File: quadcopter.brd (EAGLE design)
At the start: 247.1 x 246.9 mm, 79 parts, among them J1 ISP, U1 ATMEGA128RFA1, Y1 16MHz, Y2 32.768kHz

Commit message: Fixed Schematic but still not able to root 90%
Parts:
- removed A1: ANTENNA2SMD5, SparkFun-RF:ANTENNA-CHIP5
- removed B1: 748421245, SparkFun-RF:BALUN
- removed C24, C25: 10nF, quadparts_prebuilt:CAPC2012X140_HS
- removed C26, C28: 100nF, quadparts_prebuilt:CAPC2012X140_HS
- removed C27: 10uF, quadparts_prebuilt:CAPC2012X140_HS
- removed C6: 12pF, SparkFun-Passives:0402-CAP
- removed CG, CG1, CG2, CG3: 1uF, quadparts_prebuilt:CAPC2012X140_HS
- removed D10: Orange, quadparts_prebuilt:LEDSC125X200X120-2_HS
- removed D6: Green, quadparts_prebuilt:LEDSC125X200X120-2_HS
- removed R10, R2: 330, quadparts_prebuilt:RESC2012X60_HS
- removed R8, RG2, RG4, RG6, RG8: 10K, quadparts_prebuilt:RESC2012X60_HS
- removed RG1, RG3, RG5, RG7: 100, quadparts_prebuilt:RESC2012X60_HS
- removed U1: ATMEGA128RFA1, SparkFun-DigitalIC:QFN-64
- removed Y1: 16MHz, SparkFun-FreqCtrl:CRYSTAL-SMD-5X3
- added ANDREW1: LSM9DS1, QuadpartsUpdated:LSM9DS1
- added B2: BALUN0805, quadparts_prebuilt:BALUN
- added C13, C14, C18: 1uF, quadparts_prebuilt:CAPC2012X140_HS
- added C19, C20: 0.1uF, quadparts_prebuilt:CAPC2012X140_HS
- added C21: 0.01uF, quadparts_prebuilt:CAPC2012X140_HS
- added J7, M1, M2, M3, M4: (no value), quadparts_prebuilt:MALE_HEADER_2X1_0.1IN
- added R12, R14, R16, R18: 100, quadparts_prebuilt:RESC2012X60_HS
- added R13, R15, R17, R5, R6: 10K, quadparts_prebuilt:RESC2012X60_HS
- added U2: ATMEGA128RFA1, quadparts_prebuilt:QFN-64
- C1, C2: value 1uF -> 12pF; device SparkFun-Passives:0402-CAP -> quadparts_prebuilt:CAPC2012X140_HS
- C10: value 100nF -> 1uF
- C11: value 22pF -> 1uF; device SparkFun-Passives:0402-CAP -> quadparts_prebuilt:CAPC2012X140_HS
- C12: value 10uF -> 1uF
- C15, C4, C9: device SparkFun-Passives:0402-CAP -> quadparts_prebuilt:CAPC2012X140_HS
- C16: value JUMP -> 1uF; device SparkFun:0402-CAP -> quadparts_prebuilt:CAPC2012X140_HS
- C17: value JUMP -> 10uF; device SparkFun:0402-CAP -> quadparts_prebuilt:CAPC2012X140_HS
- C22: value 1uF -> 22pF
- C3: value 1000uF -> 1uF; device SparkFun-Passives:0402-CAP -> quadparts_prebuilt:CAPC2012X140_HS
- C5: value 12pF -> 220uF; device SparkFun-Passives:0402-CAP -> quadparts_prebuilt:CAPMP7343X310_HS
- C7: value 12pF -> 10uF; device SparkFun-Passives:0402-CAP -> quadparts_prebuilt:CAPC2012X140_HS
- C8: value 12pF -> 0.01uF; device SparkFun-Passives:0402-CAP -> quadparts_prebuilt:CAPC2012X140_HS
- R1: value 10k -> 10K; device SparkFun-Passives:0402-RES -> quadparts_prebuilt:RESC2012X60_HS
- R11: value 100 -> 10K
- U$5: value IMULAST -> ANTENNA2SMD5; device QuadpartsUpdated:LGA-24/4MM -> quadparts_prebuilt:ANTENNA-CHIP5
- Y2: value 32.768kHz -> (none); device SparkFun-FreqCtrl:CRYSTAL-32KHZ-SMD -> quadparts_prebuilt:CRYSTAL-SMD-5X3
- moved C11 288.3 mm to (-191.8, 158.8)
- moved C8 280.3 mm to (-204.5, 149.9), turned to 0 degrees
- moved C16 254.3 mm to (-139.7, 162.6)
- moved C17 251.5 mm to (-149.9, 158.8), turned to 0 degrees
- moved C15 246.9 mm to (-170.2, 154.9), flipped to the top
- moved R1 242.4 mm to (-158.8, 162.6), turned to 0 degrees
- moved C7 233.5 mm to (-142.2, 158.8), turned to 0 degrees
- moved C12 232.1 mm to (-198.1, 158.8), turned to 0 degrees
- moved C23 199.5 mm to (-152.4, 162.6), turned to 0 degrees
- moved RX_R 86.8 mm to (14.7, 28.9), flipped to the bottom, turned to 0 degrees
- moved C3 86.0 mm to (6.70, 35.0), turned to 0 degrees
- moved C4 83.6 mm to (13.4, 31.7), turned to 0 degrees
- moved RX_LED 80.7 mm to (19.1, 30.0), flipped to the bottom, turned to 270 degrees
- moved TX_LED 78.2 mm to (9.93, 30.0), flipped to the bottom, turned to 270 degrees
- moved TX_R 77.2 mm to (10.0, 24.7), flipped to the bottom
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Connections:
- removed net A0: U1.63
- removed net N$10: B1.4, C16.2
- removed net N$11: B1.3, C17.1
- removed net N$25: MOSFET3.1, RG5.1, RG6.1
- removed net N$30: MOSFET4.1, RG7.1, RG8.1
- removed net N$31: D6.A, R2.1
- removed net N$34: R8.2, U$5.5
- removed net N$35: D10.A, R10.1
- removed net N$5: C7.1, U1.18, Y2.X1
- removed net N$6: C8.1, U1.17, Y2.X2
- removed net PG5: U1.19
- removed net TST: U1.11
- new net N$48: MOSFET2.1
- new net N$50: MOSFET3.1
- new net N$52: C18.1, MOSFET4.1, R17.2, R18.2
- new net VBAT_SENSE: R5.1, R6.2, U2.63
- net 3V: now also ANDREW1.P$1, ANDREW1.P$13, ANDREW1.P$22, ANDREW1.P$23, ANDREW1.P$3, ANDREW1.P$5, ANDREW1.P$6, ANDREW1.P$7, ANDREW1.P$8, C16.1, C17.2, C19.2, J7.1, U2.23, U2.34, U2.44, U2.54, U2.59; no longer C23.1, C26.2, C27.2, R8.1, U$5.22, U$5.23, U$5.6, U$5.7, U$5.8, U1.23, U1.34, U1.44, U1.54, U1.59
- net A1: now also U2.64; no longer U1.64
- net A2: now also U2.1; no longer U1.1
- net A3: now also U2.2; no longer U1.2
- net A4: now also U2.3; no longer U1.3
- net A5: now also U2.4; no longer U1.4
- net A6: now also U2.5; no longer U1.5
- net A7: now also U2.6; no longer U1.6
- net AREF: now also U2.62; no longer U1.62
- net AVDD: now also C11.1, U2.60; no longer C1.1, U1.60
- net BAT_GND: now also C5.2, C7.2, C8.2; no longer C12.2, C24.2, D10.C, D6.C, R11.1
- net DVDD: now also C23.1, U2.21, U2.22; no longer C2.1, U1.21, U1.22
- net GND: now also ANDREW1.P$14, ANDREW1.P$15, ANDREW1.P$16, ANDREW1.P$17, ANDREW1.P$18, ANDREW1.P$19, ANDREW1.P$20, B2.5, C12.2, C13.2, C14.2, C16.2, C17.1, C18.2, C19.1, C20.1, C21.2, C22.1, C9.2, J7.2, M1.1, M2.1, M3.1, M4.1, R11.1, R13.1, R15.1, R17.1, R6.1, U2.10, U2.11, U2.20, U2.24, U2.33, U2.35, U2.45, U2.55, U2.58, U2.61, U2.7; no longer B1.5, C22.2, C25.2, C26.1, C27.1, C28.1, C5.2, C6.2, C7.2, C8.2, C9.1, CG.2, CG1.2, CG2.2, CG3.2, R11.2, RG2.2, RG4.2, RG6.2, RG8.2, U$5.14, U$5.15, U$5.16, U$5.17, U$5.18\, U$5.19, U$5.20, U1.10, U1.20, U1.24, U1.33, U1.35, U1.45, U1.55, U1.58, U1.61, U1.65, U1.7
- net MISO: now also U2.39; no longer U1.39
- net MOSI: now also U2.38; no longer U1.38
- net N$15: now also C13.1, R13.2, R14.2; no longer MOSFET1.1, RG1.1, RG2.1
- net N$2: now also MOSFET1.1, R11.2, R12.2; no longer U$5.1, U$5.3
- net N$20: now also C14.1, R15.2, R16.2; no longer MOSFET2.1, RG3.1, RG4.1
- net N$23: now also ANDREW1.P$24, C20.2; no longer C28.2, U$5.24
- net N$26: now also C12.1; no longer C22.1
- net N$3: now also C2.1, U2.57, Y2.3; no longer C5.1, U1.57, Y1.3
- net N$33: now also ANDREW1.P$21, C21.1; no longer C25.1, U$5.21
- net N$4: now also C1.1, U2.56, Y2.1; no longer C6.1, U1.56, Y1.1
- net N$7: now also B2.2, C22.2; no longer B1.2, C11.1
- net PB4: now also U2.40; no longer U1.40
- net PB6: now also U2.42; no longer U1.42
- net PB7: now also U2.43; no longer U1.43
- net PD4: now also U2.29; no longer U1.29
- net PD5: now also U2.30; no longer U1.30
- net PD6: now also U2.31; no longer U1.31
- net PD7: now also U2.32; no longer U1.32
- net PE2: now also U2.48; no longer U1.48
- net PE6: now also U2.52; no longer U1.52
- net PE7: now also U2.53; no longer U1.53
- net PG0: now also U2.14; no longer U1.14
- net PG1: now also U2.15; no longer U1.15
- net PG2: now also U2.16; no longer U1.16
- net PWM1: now also M1.2, R12.1, U2.41; no longer CG.1, RG1.2, U1.41
- net PWM2: now also M2.2, R14.1, U2.51; no longer CG1.1, RG3.2, U1.51
- net PWM3: now also M3.2, R16.1, U2.49; no longer CG2.1, RG5.2, U1.49
- net PWM4: now also M4.2, R18.1, U2.50; no longer CG3.1, RG7.2, U1.50
- net RESET: now also U2.12; no longer U1.12
- net RFANT: now also B2.1, C9.1, U$5.FEED; no longer A1.FEED, B1.1, C9.2
- net RFN: now also B2.3, U2.9; no longer C17.2, U1.9
- net RFP: now also B2.4, U2.8; no longer C16.1, U1.8
- net RSTON: now also U2.13; no longer U1.13
- net RX0: now also SERIAL_PROGRAMMER.TXO, U2.46; no longer U1.46
- net RX1: now also U2.27; no longer SERIAL_PROGRAMMER.TXO, U1.27
- net SCK: now also U2.37; no longer U1.37
- net SCL: now also ANDREW1.P$2, U2.25; no longer U$5.2, U1.25
- net SDA: now also ANDREW1.P$4, U2.26; no longer U$5.4, U1.26
- net SSN: now also U2.36; no longer U1.36
- net TX0: now also SERIAL_PROGRAMMER.RXI, U2.47; no longer U1.47
- net TX1: now also U2.28; no longer SERIAL_PROGRAMMER.RXI, U1.28
- net VBAT: now also C5.1, C7.1, C8.1, R5.2; no longer C12.1, C24.1, R10.2, R2.2
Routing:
- net GND: track 395.9 -> 0.00 mm, vias 7 -> 0
- net 3V: track 326.6 -> 0.00 mm, vias 7 -> 0
- net VBAT: track 303.3 -> 0.00 mm, vias 5 -> 0
- net PWM2: track 192.4 -> 0.00 mm, vias 1 -> 0
- net RX1: track 133.9 -> 0.00 mm, vias 2 -> 0
- net BAT_GND: track 133.8 -> 0.00 mm
- net TX1: track 133.6 -> 0.00 mm, vias 2 -> 0
- net PWM1: track 129.9 -> 0.00 mm, vias 2 -> 0
- net RESET: track 124.0 -> 0.00 mm, vias 1 -> 0
- net PWM4: track 110.5 -> 0.00 mm, vias 1 -> 0
- net PWM3: track 104.1 -> 0.00 mm
- net SDA: track 96.3 -> 0.00 mm, vias 3 -> 0
- net SCL: track 92.0 -> 0.00 mm, vias 2 -> 0
- net N$6: track 72.7 -> 0.00 mm
- net AVDD: track 50.7 -> 0.00 mm, vias 1 -> 0
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- removed copper zone on layer 2, net 3V
- removed copper zone on layer 15, net GND
- removed copper zone on layer 2, net GND
- removed copper zone on layer 2, net VBAT
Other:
- board size 247.1 x 246.9 mm -> 130.1 x 130.4 mm

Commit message: Route 100% FINALLY.
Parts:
- removed ANDREW1: LSM9DS1, QuadpartsUpdated:LSM9DS1
- added R2, R8: 10K, quadparts_prebuilt:RESC2012X60_HS
- added U$6: IMULAST, QuadpartsUpdated:LGA-24/4MM
- added U$7: WIRE_BRIDGE, QuadpartsUpdated:WIRE_BRIGE
- moved C15 251.4 mm to (4.20, -26.1), turned to 90 degrees
- moved C11 247.1 mm to (-16.4, -15.3), turned to 90 degrees
- moved C20 237.5 mm to (1.10, 7.90), flipped to the bottom, turned to 270 degrees
- moved C23 235.7 mm to (-18.2, -31.2), turned to 90 degrees
- moved C8 235.6 mm to (-4.60, 25.1), turned to 90 degrees
- moved C12 229.5 mm to (-15.1, 20.3), turned to 180 degrees
- moved R6 221.6 mm to (-15.3, 26.9), turned to 180 degrees
- moved R5 218.6 mm to (-15.2, 23.9)
- moved C21 206.2 mm to (-1.30, 8.10), flipped to the bottom, turned to 90 degrees
- moved C19 205.6 mm to (-22.6, 20.1)
- moved R1 199.1 mm to (-22.6, 17.3)
- moved C17 195.6 mm to (-15.0, 17.1)
- moved C7 189.9 mm to (-7.50, 25.0), turned to 90 degrees
- moved C16 181.9 mm to (-15.3, 29.8), turned to 180 degrees
- moved B2 65.7 mm to (-22.6, -25.4), turned to 90 degrees
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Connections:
- removed net AREF: U2.62
- net 3V: now also R2.2, R8.2, U$6.1, U$6.13, U$6.22, U$6.23, U$6.3, U$6.5, U$6.6, U$6.7, U$6.8, U2.62; no longer ANDREW1.P$1, ANDREW1.P$13, ANDREW1.P$22, ANDREW1.P$23, ANDREW1.P$3, ANDREW1.P$5, ANDREW1.P$6, ANDREW1.P$7, ANDREW1.P$8
- net BAT_GND: now also U$7.GND
- net GND: now also U$6.14, U$6.15, U$6.16, U$6.17, U$6.18\, U$6.19, U$6.20, U$7.BATT_GND; no longer ANDREW1.P$14, ANDREW1.P$15, ANDREW1.P$16, ANDREW1.P$17, ANDREW1.P$18, ANDREW1.P$19, ANDREW1.P$20
- net N$23: now also U$6.24; no longer ANDREW1.P$24
- net N$33: now also U$6.21; no longer ANDREW1.P$21
- net SCL: now also R8.1, U$6.2; no longer ANDREW1.P$2
- net SDA: now also R2.1, U$6.4; no longer ANDREW1.P$4
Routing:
- net VBAT: track 0.00 -> 300.1 mm, vias 0 -> 2
- net GND: track 0.00 -> 280.3 mm, vias 0 -> 16
- net 3V: track 0.00 -> 191.3 mm, vias 0 -> 5
- net BAT_GND: track 0.00 -> 118.3 mm, vias 0 -> 1
- net RESET: track 0.00 -> 113.3 mm, vias 0 -> 4
- net PWM2: track 0.00 -> 95.9 mm, vias 0 -> 2
- net RX0: track 0.00 -> 93.3 mm, vias 0 -> 2
- net TX0: track 0.00 -> 89.8 mm, vias 0 -> 2
- net PWM1: track 0.00 -> 85.8 mm, vias 0 -> 2
- net SCL: track 0.00 -> 74.7 mm, vias 0 -> 4
- net SDA: track 0.00 -> 74.4 mm, vias 0 -> 3
- net PWM4: track 0.00 -> 63.0 mm, vias 0 -> 1
- net PWM3: track 0.00 -> 57.7 mm
- net VBAT_SENSE: track 0.00 -> 50.5 mm, vias 0 -> 2
- net RX1: track 0.00 -> 50.1 mm
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- added copper zone on layer 2, net 3V
- added copper zone on layer 15, net GND
- added copper zone on layer 2, net VBAT
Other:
- outline, holes or cut-outs redrawn

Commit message: After fixing professor's comments
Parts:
- removed C7: 10uF, quadparts_prebuilt:CAPC2012X140_HS
- removed C8: 0.01uF, quadparts_prebuilt:CAPC2012X140_HS
- added C6: 0.1uF, quadparts_prebuilt:CAPC2012X140_HS
- C10, C13, C14: value 1uF -> 0.1uF
- D1, D2, D3, D4: value (none) -> 360mV
- moved C10 73.1 mm to (31.3, 4.38), turned to 90 degrees
- moved C18 69.3 mm to (2.67, 28.1), turned to 90 degrees
- moved C13 55.6 mm to (-31.9, -5.44), turned to 270 degrees
- moved BREAKOUT_HEADER 54.2 mm to (-28.6, -14.2), turned to 90 degrees
- moved C14 51.7 mm to (1.21, 35.0), turned to 0 degrees
- moved R6 36.0 mm to (-15.3, -9.11), turned to 270 degrees
- moved R5 33.1 mm to (-17.8, -9.06), turned to 90 degrees
- moved U$7 21.9 mm to (-5.00, 16.6), turned to 180 degrees
- moved C15 20.3 mm to (-15.5, -30.9)
- moved C1 13.9 mm to (-6.32, -7.89), turned to 0 degrees
- moved C21 13.9 mm to (-1.84, -5.79), flipped to the top, turned to 270 degrees
- moved C20 13.6 mm to (0.28, -5.72), flipped to the top, turned to 90 degrees
- moved SWRESET 7.84 mm to (-29.0, 17.0)
- moved C22 7.47 mm to (-21.4, -27.0), turned to 0 degrees
- moved C23 7.41 mm to (-10.9, -32.7), turned to 270 degrees
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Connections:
- removed net N$15: C13.1, R13.2, R14.2
- removed net N$20: C14.1, R15.2, R16.2
- net BAT_GND: now also C10.2, C13.2, C14.2, C18.2, C6.2, M1.1, M2.1, M3.1, M4.1, MOSFET1.2, MOSFET2.2, MOSFET3.2, MOSFET4.2, R11.1, R13.1, R15.1, R17.1; no longer C7.2, C8.2
- net GND: no longer C10.2, C13.2, C14.2, C18.2, M1.1, M2.1, M3.1, M4.1, MOSFET1.2, MOSFET2.2, MOSFET3.2, MOSFET4.2, R11.1, R13.1, R15.1, R17.1
- net N$2: now also C13.1; no longer C10.1
- net N$48: now also C14.1, R13.2, R14.2
- net N$50: now also C10.1, R15.2, R16.2
- net N$52: now also C6.1; no longer C18.1
- net VBAT: now also C18.1; no longer C7.1, C8.1
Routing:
- net BAT_GND: track 118.3 -> 295.0 mm, vias 1 -> 9
- net VBAT: track 300.1 -> 131.1 mm, vias 2 -> 8
- net GND: track 280.3 -> 192.6 mm, vias 16 -> 8
- net VBAT_SENSE: track 50.5 -> 13.7 mm, vias 2 -> 0
- net N$50: track 0.00 -> 32.6 mm
- net PWM3: track 57.7 -> 87.2 mm, vias 0 -> 4
- net N$48: track 0.00 -> 24.4 mm
- net SCL: track 74.7 -> 97.0 mm
- net PWM2: track 95.9 -> 115.5 mm
- net SDA: track 74.4 -> 93.7 mm, vias 3 -> 2
- net DTR: track 9.48 -> 28.8 mm
- net RX0: track 93.3 -> 111.3 mm
- net PWM1: track 85.8 -> 68.6 mm
- net N$4: track 26.3 -> 10.4 mm, vias 2 -> 0
- net RFANT: track 25.3 -> 9.60 mm, vias 2 -> 0
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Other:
- board size 130.1 x 130.4 mm -> 134.1 x 134 mm

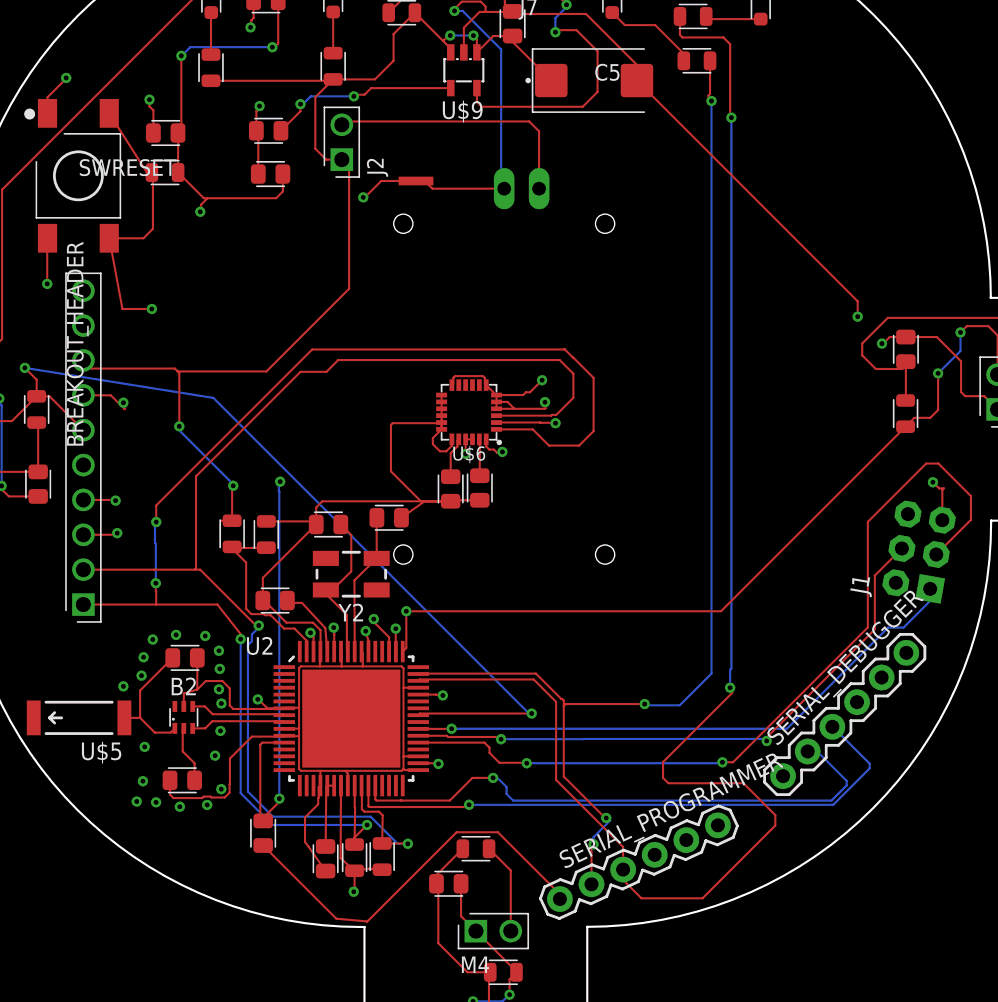
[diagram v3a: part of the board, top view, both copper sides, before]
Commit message: After fixing professor's comments V2
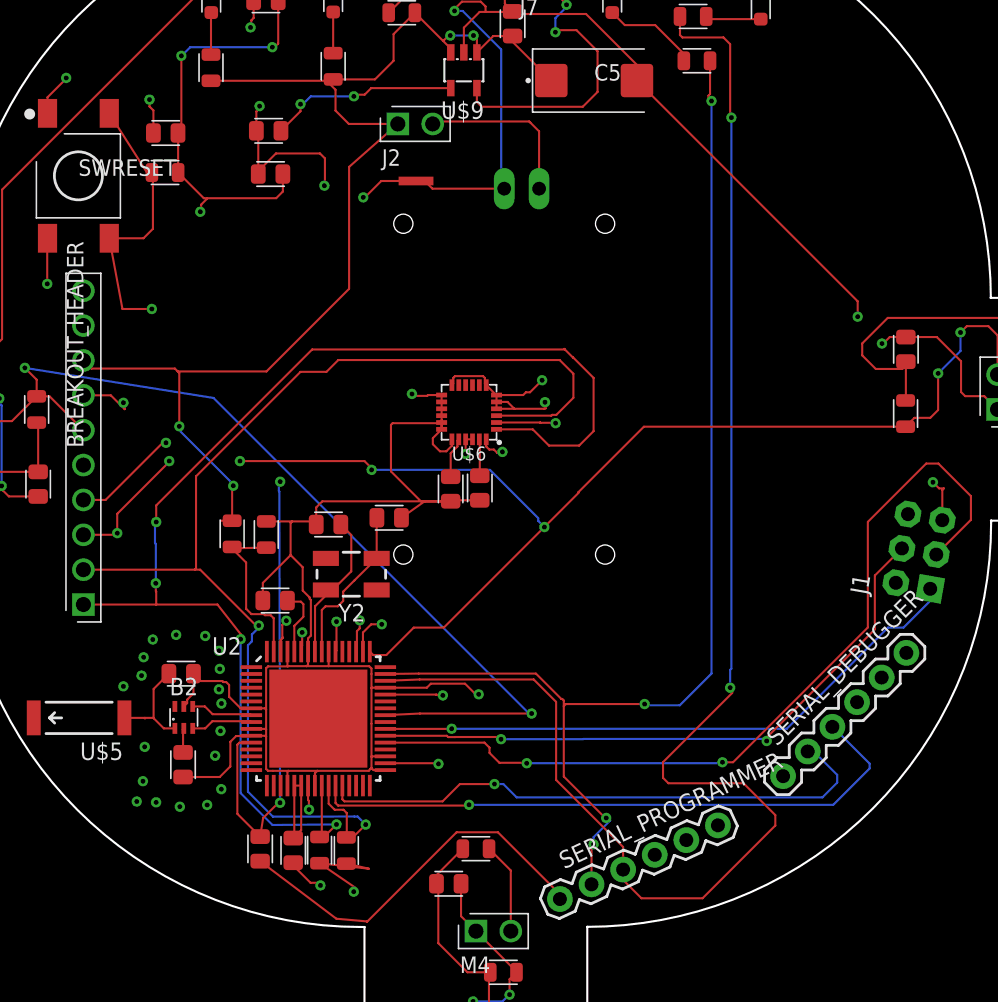
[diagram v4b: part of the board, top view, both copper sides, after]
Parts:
- moved J2 4.84 mm to (-5.69, 20.8), turned to 0 degrees
- moved R2 2.65 mm to (-9.44, -32.1)
- moved R8 2.61 mm to (-11.4, -32.1)
- moved C23 2.44 mm to (-13.3, -32.1)
- moved U2 2.40 mm to (-11.5, -22.5)
- moved C9 1.18 mm to (-21.5, -19.2)
- moved C15 1.16 mm to (-15.7, -32.0)
- moved C22 1.14 mm to (-21.3, -25.9), turned to 90 degrees
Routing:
- net VBAT: track 131.1 -> 185.0 mm
- net PWM4: track 64.4 -> 106.5 mm, vias 2 -> 3
- net GND: track 192.6 -> 231.9 mm, vias 8 -> 11
- net 3V: track 179.1 -> 198.6 mm, vias 20 -> 21
- net PWM3: track 87.2 -> 99.9 mm, vias 4 -> 6
- net N$17: track 18.9 -> 12.3 mm
- net SDA: track 93.7 -> 89.1 mm
- net DVDD: track 4.96 -> 8.25 mm
- net SCL: track 97.0 -> 94.1 mm
- net RESET: track 121.6 -> 124.2 mm
- net SCK: track 61.0 -> 63.4 mm
- net RFP: track 6.93 -> 4.53 mm
- net RFN: track 6.91 -> 4.51 mm
- net MOSI: track 43.7 -> 46.1 mm
- net MISO: track 42.1 -> 44.5 mm
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
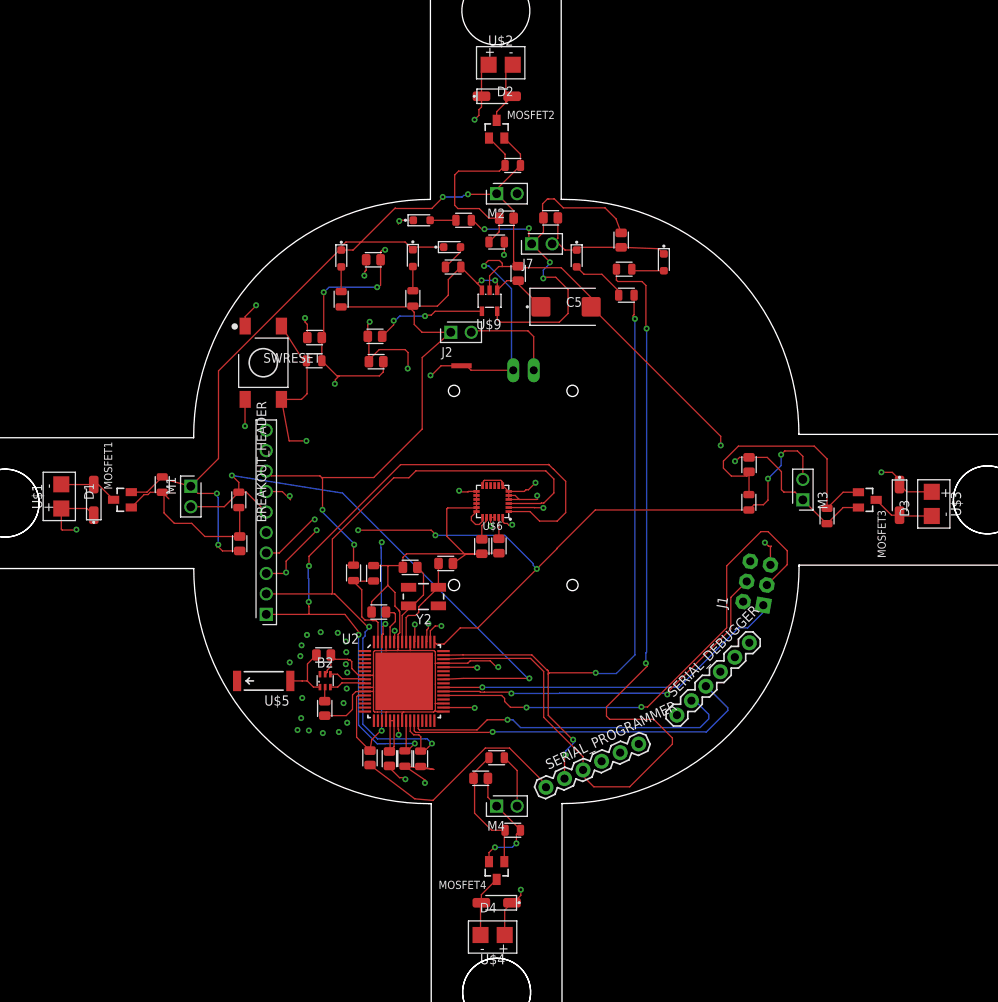
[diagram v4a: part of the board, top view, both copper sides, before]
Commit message: After fixing professor's comments V2
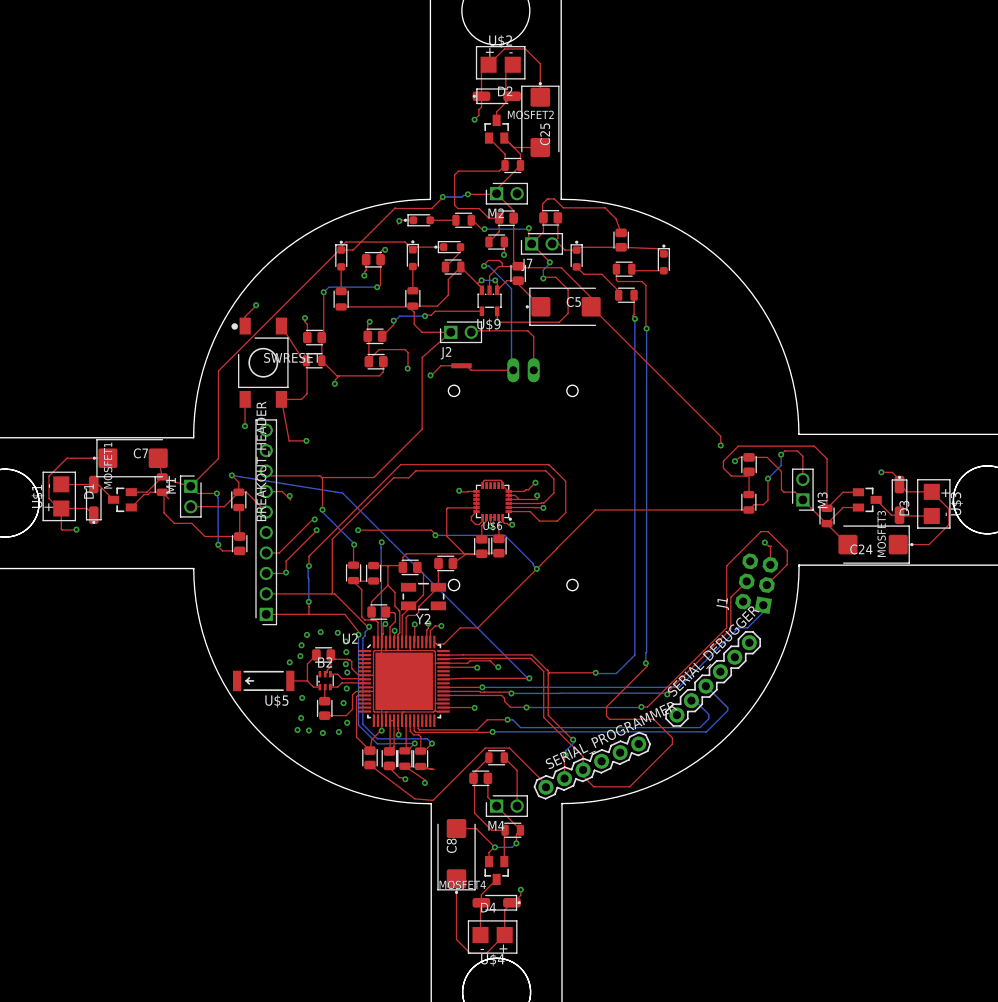
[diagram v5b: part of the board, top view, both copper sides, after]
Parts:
- added C24, C25, C7, C8: 220uF, quadparts_prebuilt:CAPMP7343X310_HS
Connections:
- net BAT_GND: now also C24.2, C25.2, C7.2, C8.2
- net VBAT: now also C24.1, C25.1, C7.1, C8.1
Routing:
- net VBAT: track 185.0 -> 237.7 mm
- net BAT_GND: track 295.0 -> 307.1 mm
- net PWM2: track 114.0 -> 110.9 mm
- added copper zone on layer 15, net BAT_GND
